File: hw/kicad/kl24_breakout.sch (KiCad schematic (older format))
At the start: 26 parts

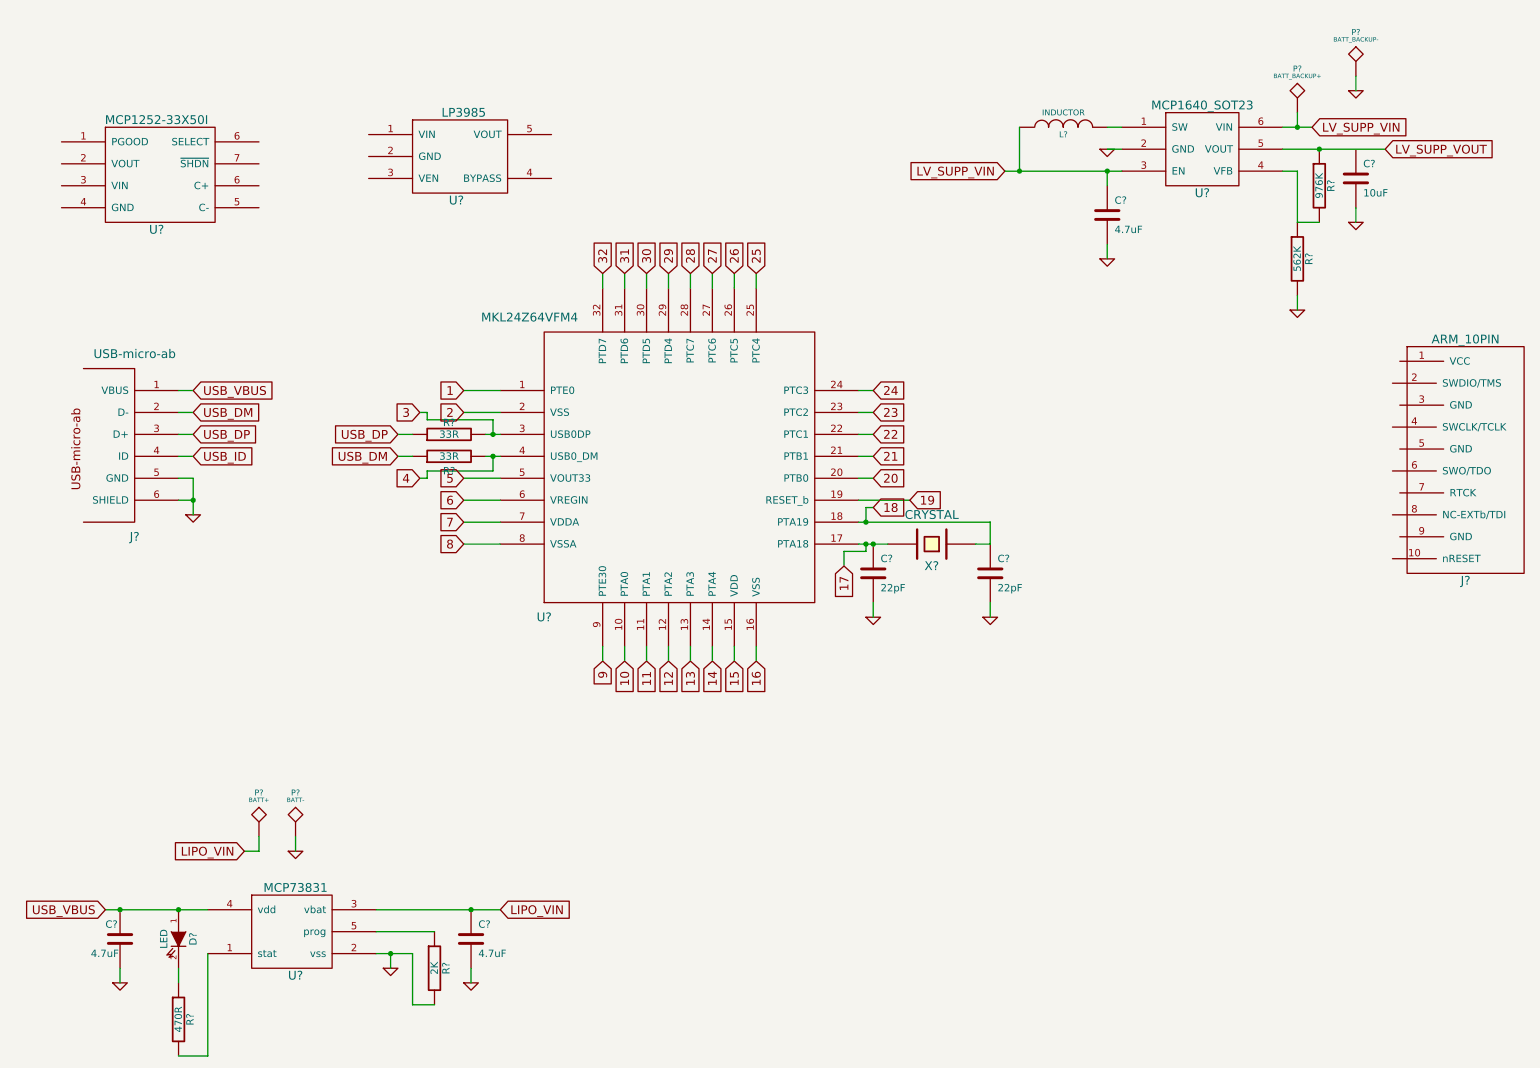
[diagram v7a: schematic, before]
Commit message: - add some labels to submodules in the schematic
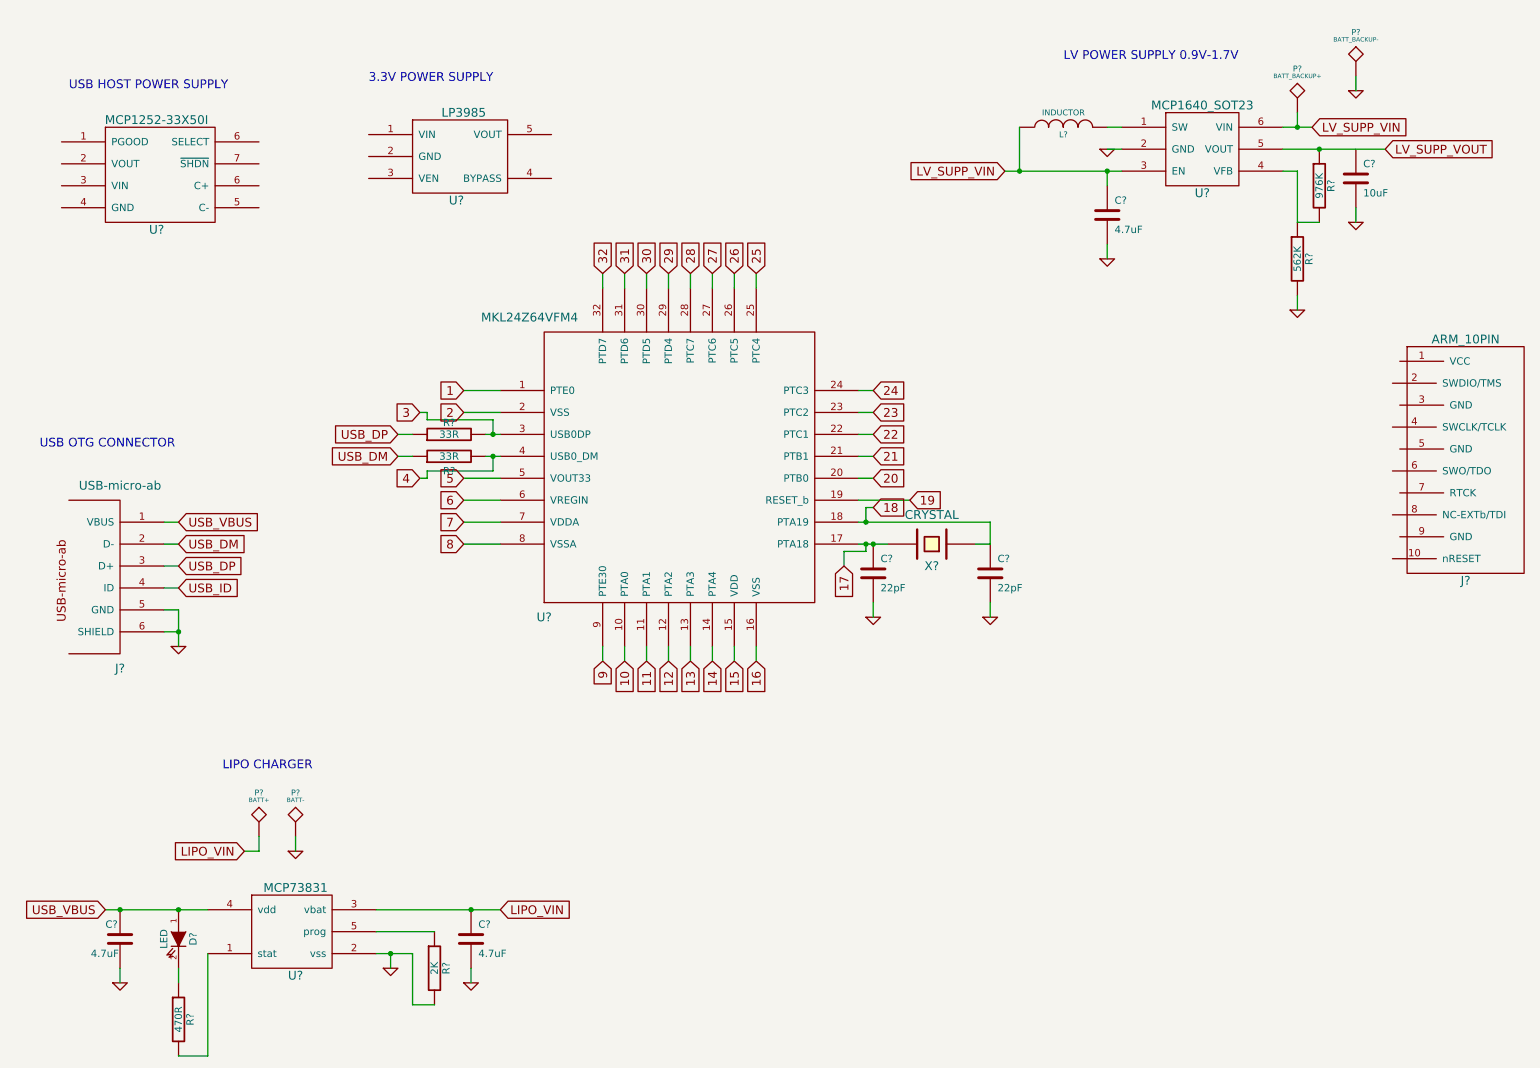
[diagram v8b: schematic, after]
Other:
- note added: "3.3V POWER SUPPLY"
- note added: "LIPO CHARGER"
- note added: "LV POWER SUPPLY 0.9V-1.7V"
- note added: "USB HOST POWER SUPPLY"
- note added: "USB OTG CONNECTOR"
- moved on the sheet: J?
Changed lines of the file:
@@
-EESchema Schematic File Version 2  date 3/9/2013 9:06:54 PM
+EESchema Schematic File Version 2  date 3/12/2013 3:35:46 PM
 LIBS:power
 LIBS:device
@@
 Sheet 1 1
 Title ""
-Date "10 mar 2013"
+Date "12 mar 2013"
 Rev ""
 Comp ""
@@
 	1350 6950 1350 7050
 Wire Wire Line
-	1850 3000 1750 3000
-Wire Wire Line
-	1850 3300 1750 3300
+	1750 3900 1650 3900
+Wire Wire Line
+	1750 4200 1650 4200
 Wire Wire Line
 	3200 6850 3200 6950
@@
 Wire Wire Line
 	9500 1200 9300 1200
-Connection ~ 1850 3750
-Wire Wire Line
-	1850 3850 1850 3600
-Wire Wire Line
-	1850 3600 1750 3600
+Connection ~ 1750 4650
+Wire Wire Line
+	1750 4750 1750 4500
+Wire Wire Line
+	1750 4500 1650 4500
 Wire Wire Line
 	2550 6150 2550 6050
@@
 	9800 850  9800 950
 Wire Wire Line
-	1850 3750 1750 3750
+	1750 4650 1650 4650
 Wire Wire Line
 	9400 1200 9400 1100
@@
 Connection ~ 7500 1500
 Wire Wire Line
-	1750 3450 1850 3450
-Wire Wire Line
-	1750 3150 1850 3150
+	1650 4350 1750 4350
+Wire Wire Line
+	1650 4050 1750 4050
 Connection ~ 1350 6550
 Wire Wire Line
@@
 Text GLabel 1250 6550 0    60   Input ~ 0
 USB_VBUS
-Text GLabel 1850 3450 2    60   Input ~ 0
+Text GLabel 1750 4350 2    60   Input ~ 0
 USB_ID
-Text GLabel 1850 3300 2    60   Input ~ 0
+Text GLabel 1750 4200 2    60   Input ~ 0
 USB_DP
-Text GLabel 1850 3150 2    60   Input ~ 0
+Text GLabel 1750 4050 2    60   Input ~ 0
 USB_DM
-Text GLabel 1850 3000 2    60   Input ~ 0
+Text GLabel 1750 3900 2    60   Input ~ 0
 USB_VBUS
 $Comp
@@
 L GND #PWR?
 U 1 1 513B6B06
-P 1850 3850
-F 0 "#PWR?" H 1850 3850 30  0001 C CNN
-F 1 "GND" H 1850 3780 30  0001 C CNN
-F 2 "" H 1850 3850 60  0001 C CNN
-F 3 "" H 1850 3850 60  0001 C CNN
-	1    1850 3850
+P 1750 4750
+F 0 "#PWR?" H 1750 4750 30  0001 C CNN
+F 1 "GND" H 1750 4680 30  0001 C CNN
+F 2 "" H 1750 4750 60  0001 C CNN
+F 3 "" H 1750 4750 60  0001 C CNN
+	1    1750 4750
 	1    0    0    -1
 $EndComp
@@
 L USB-micro-ab J?
 U 1 1 5135355A
-P 1450 3400
-F 0 "J?" H 1450 2800 60  0000 C CNN
-F 1 "USB-micro-ab" H 1450 4050 60  0000 C CNN
-F 2 "" H 1450 3400 60  0001 C CNN
-F 3 "" H 1450 3400 60  0001 C CNN
-	1    1450 3400
+P 1350 4300
+F 0 "J?" H 1350 3700 60  0000 C CNN
+F 1 "USB-micro-ab" H 1350 4950 60  0000 C CNN
+F 2 "" H 1350 4300 60  0001 C CNN
+F 3 "" H 1350 4300 60  0001 C CNN
+	1    1350 4300
 	1    0    0    -1
 $EndComp
@@
 Wire Wire Line
 	5700 2200 5700 2300
+Text Notes 2050 5600 0    60   ~ 0
+LIPO CHARGER
+Text Notes 7800 750  0    60   ~ 0
+LV POWER SUPPLY 0.9V-1.7V
+Text Notes 800  3400 0    60   ~ 0
+USB OTG CONNECTOR
+Text Notes 1000 950  0    60   ~ 0
+USB HOST POWER SUPPLY
+Text Notes 3050 900  0    60   ~ 0
+3.3V POWER SUPPLY
 $EndSCHEMATC
